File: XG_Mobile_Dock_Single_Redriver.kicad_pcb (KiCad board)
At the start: 6 copper layers, 220.1 x 93 mm, 154 parts, among them J1 5-1775443-8, J10 SWD, J11 UART, J12 I2C1, J13 39301240, J14 I2C1, J2 20455-040E-76, J3 20455-040E-76, J4 469911008, J7 CEE016400140111, Q16 AO3401A, Q17 2N7002W, SW1 SW_Push, U1 DS320PR810NJXR, U12 STM32F030C8Tx, U7 TPS7A8400ARGRR, U8 TPS7A8400ARGRR

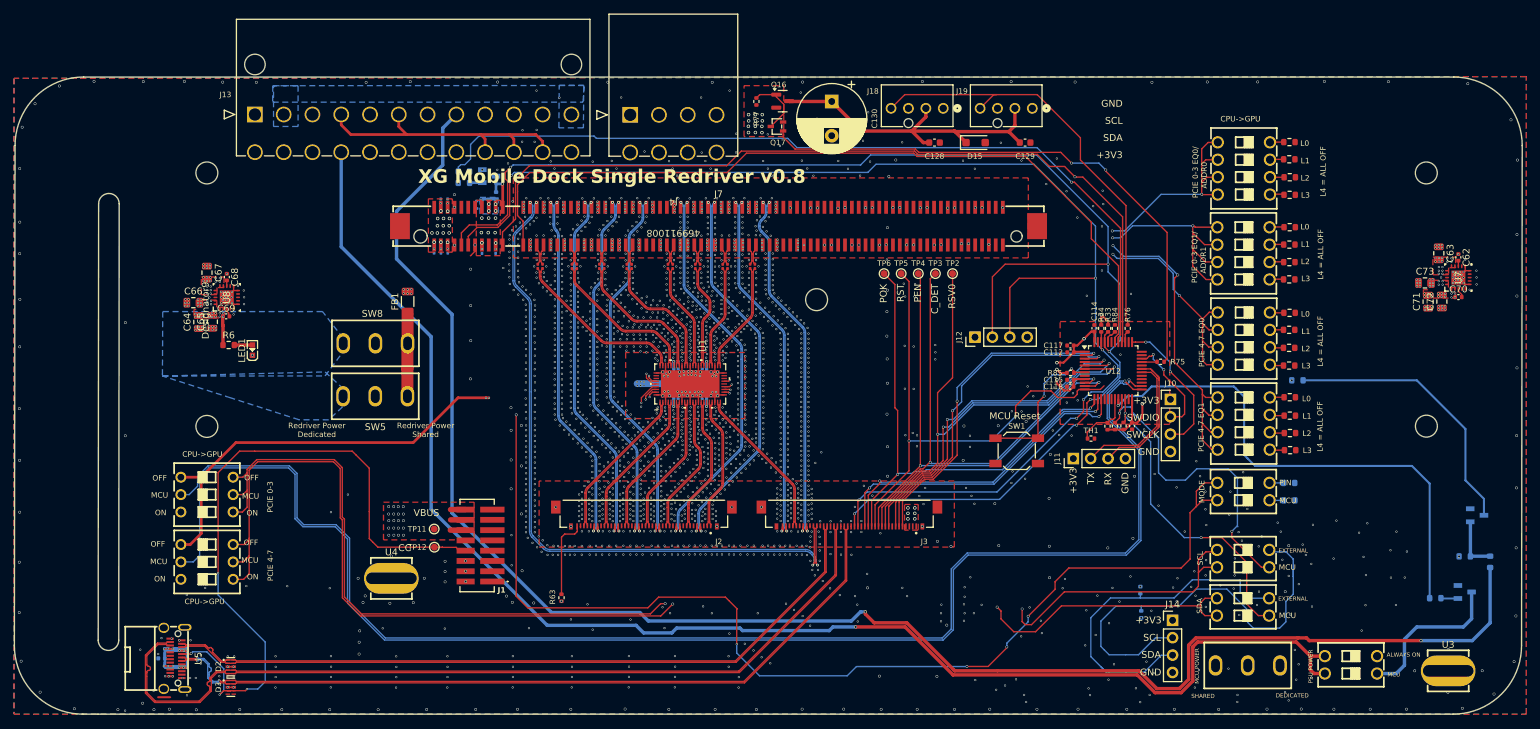
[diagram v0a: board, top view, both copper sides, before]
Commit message: Update XG_Mobile_Dock_Single_Redriver.kicad_pcb
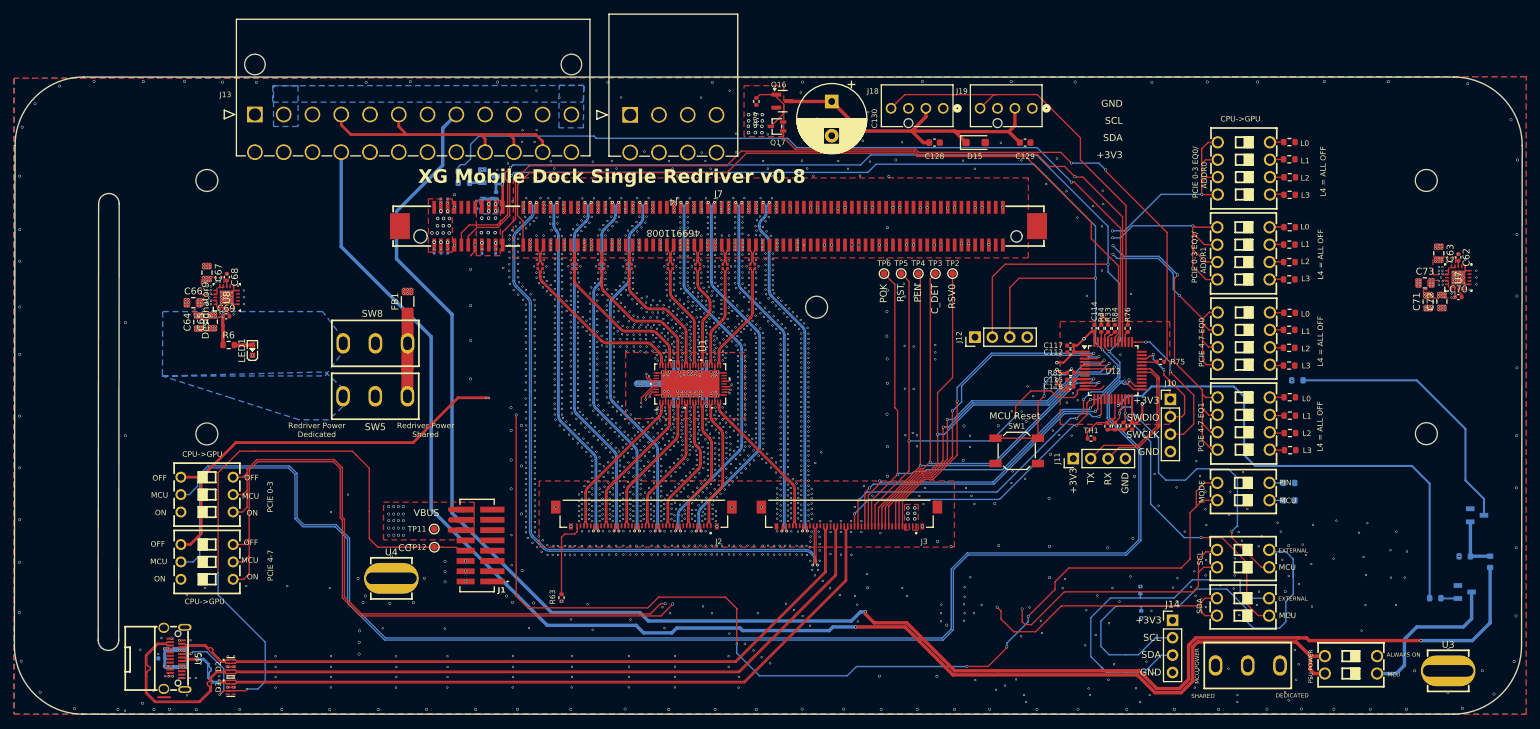
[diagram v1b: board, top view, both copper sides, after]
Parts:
- moved REF** 1.10 mm to (24.0, 99.8)
- moved REF** 1.10 mm to (44.8, 54.5)
- moved REF** 1.10 mm to (24.0, 59.2)
- moved REF** 1.10 mm to (222.8, 54.5)
- moved REF** 1.10 mm to (133.8, 73.0)
- moved REF** 1.10 mm to (222.8, 91.5)
- moved REF** 1.10 mm to (24.0, 79.5)
- moved REF** 1.10 mm to (44.8, 91.5)
